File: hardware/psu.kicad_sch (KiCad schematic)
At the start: 15 parts, among them U701 XC6206

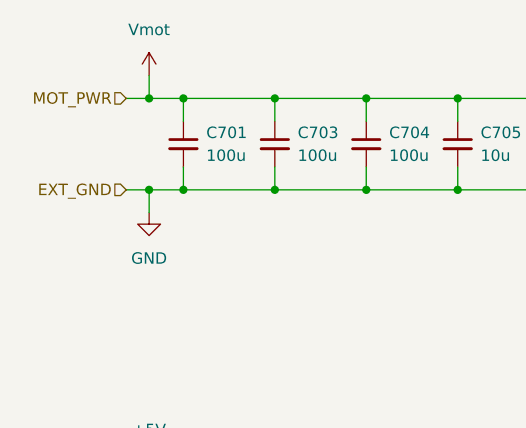
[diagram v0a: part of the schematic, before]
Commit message: update schematic (Vref+ tie to Vdd) and go through ERC check
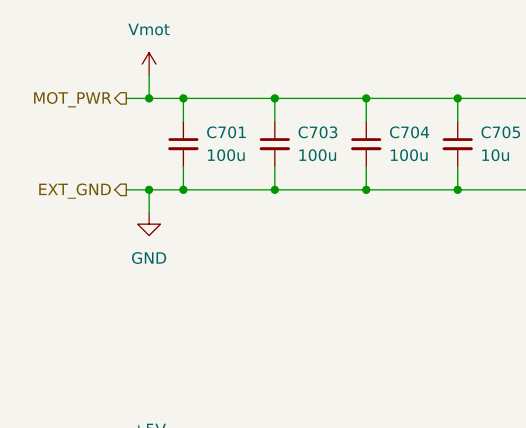
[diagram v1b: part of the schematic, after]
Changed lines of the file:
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@@
     (stroke (width 0) (type default))
   )
-  (hierarchical_label "EXT_GND" (shape input) (at 118.11 72.39 180) (fields_autoplaced)
+  (hierarchical_label "EXT_GND" (shape output) (at 118.11 72.39 180) (fields_autoplaced)
     (effects (font (size 1.27 1.27)) (justify right))
   )
-  (hierarchical_label "MOT_PWR" (shape input) (at 118.11 62.23 180) (fields_autoplaced)
+  (hierarchical_label "MOT_PWR" (shape output) (at 118.11 62.23 180) (fields_autoplaced)
     (effects (font (size 1.27 1.27)) (justify right))
   )

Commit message: update schematic to remove debounce cap
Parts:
- JP701: now left out of the parts list
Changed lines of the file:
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@@
   )
   (symbol (lib_id "Jumper:SolderJumper_2_Bridged") (at 173.99 62.23 0) (unit 1)
-    (in_bom yes) (on_board yes) (dnp no) (fields_autoplaced)
+    (in_bom no) (on_board yes) (dnp no) (fields_autoplaced)
     (property "Reference" "JP701" (at 173.99 55.88 0)
       (effects (font (size 1.27 1.27)))
